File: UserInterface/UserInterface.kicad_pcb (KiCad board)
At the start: 2 copper layers, 102.2 x 65.5 mm, 30 parts, among them J1 Conn_01x18_Pin, SW0 RotaryEncoder_Switch_MP, SW1 SW_SPST, SW2 SW_SPST, SW3 SW_SPST, SW4 SW_SPST

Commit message: add main PCB
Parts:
- moved CSW4 22.0 mm to (153.5, 129.9)
- moved RSW4 22.0 mm to (153.5, 122.9)
- moved CSW3 20.8 mm to (147.3, 129.9)
- moved RSW3 20.8 mm to (147.3, 122.9)
- moved CSW2 19.5 mm to (141.0, 130.1)
- moved RSW2 19.5 mm to (141.0, 123.0)
- moved CSW0 19.5 mm to (117.0, 130.0)
- moved RSW0 19.5 mm to (117.0, 123.0)
- moved CSW1 18.5 mm to (135.0, 130.1)
- moved RSW1 18.5 mm to (135.0, 123.0)
- moved CSW0B1 18.5 mm to (123.0, 130.0)
- moved RSW0B1 18.5 mm to (123.0, 123.0)
- moved CSW0A1 17.5 mm to (129.0, 130.0)
- moved RSW0A1 17.5 mm to (129.0, 123.0)
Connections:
- J1 pad 10: /BUTTON_3 -> /RE_B
- J1 pad 11: /BUTTON_4 -> /LED_A
- J1 pad 12: /RE_SW -> /LED_B
- J1 pad 13: /RE_A -> /BUTTON_1
- J1 pad 14: /RE_B -> /BUTTON_2
- J1 pad 15: /LED_A -> /BUTTON_3
- J1 pad 16: /LED_B -> /BUTTON_4
- J1 pad 8: /BUTTON_1 -> /RE_SW
- J1 pad 9: /BUTTON_2 -> /RE_A
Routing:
- net GND: track 335.2 -> 235.7 mm, vias 3 -> 0
- net +5V: track 170.7 -> 82.8 mm, vias 1 -> 2
- net /RE_SW: track 37.2 -> 72.4 mm
- net /BUTTON_1: track 42.5 -> 69.1 mm
- net /BUTTON_2: track 28.3 -> 50.4 mm
- net /RE_A: track 65.9 -> 87.8 mm
- net /RE_B: track 53.2 -> 72.4 mm
- net /CS: track 54.8 -> 69.2 mm
- net /RES: track 53.9 -> 67.0 mm
- net /D: track 53.1 -> 64.6 mm
- net /LED_B: track 25.1 -> 35.2 mm, vias 1 -> 0
- net /SCK: track 52.2 -> 62.1 mm
- net /LED_A: track 23.1 -> 32.0 mm, vias 1 -> 0
- net /MOSI: track 51.6 -> 60.3 mm
- net /BUTTON_3: track 27.3 -> 35.9 mm
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
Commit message: ready to fix ui pcb
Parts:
- removed J1: Conn_01x18_Pin, Connector_PinHeader_2.54mm:PinHeader_1x18_P2.54mm_Vertical
- added J2: Conn_01x08_Pin, JST:JST-XH-08-PACKAGE-LONG-PAD, F.Cu at (71.1, 120.0)
- added J3: Conn_01x08_Pin, JST:JST-XH-08-PACKAGE-LONG-PAD, F.Cu at (71.1, 127.0)

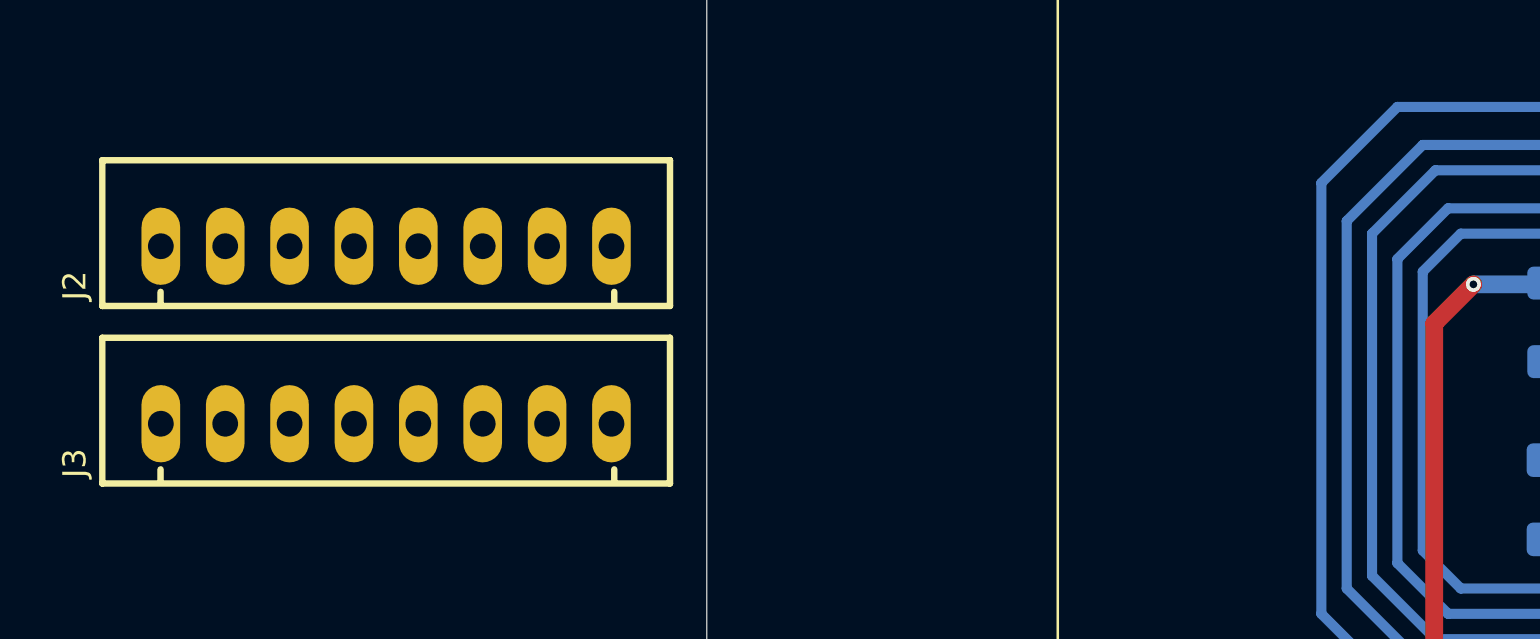
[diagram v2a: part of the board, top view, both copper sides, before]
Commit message: add step ui
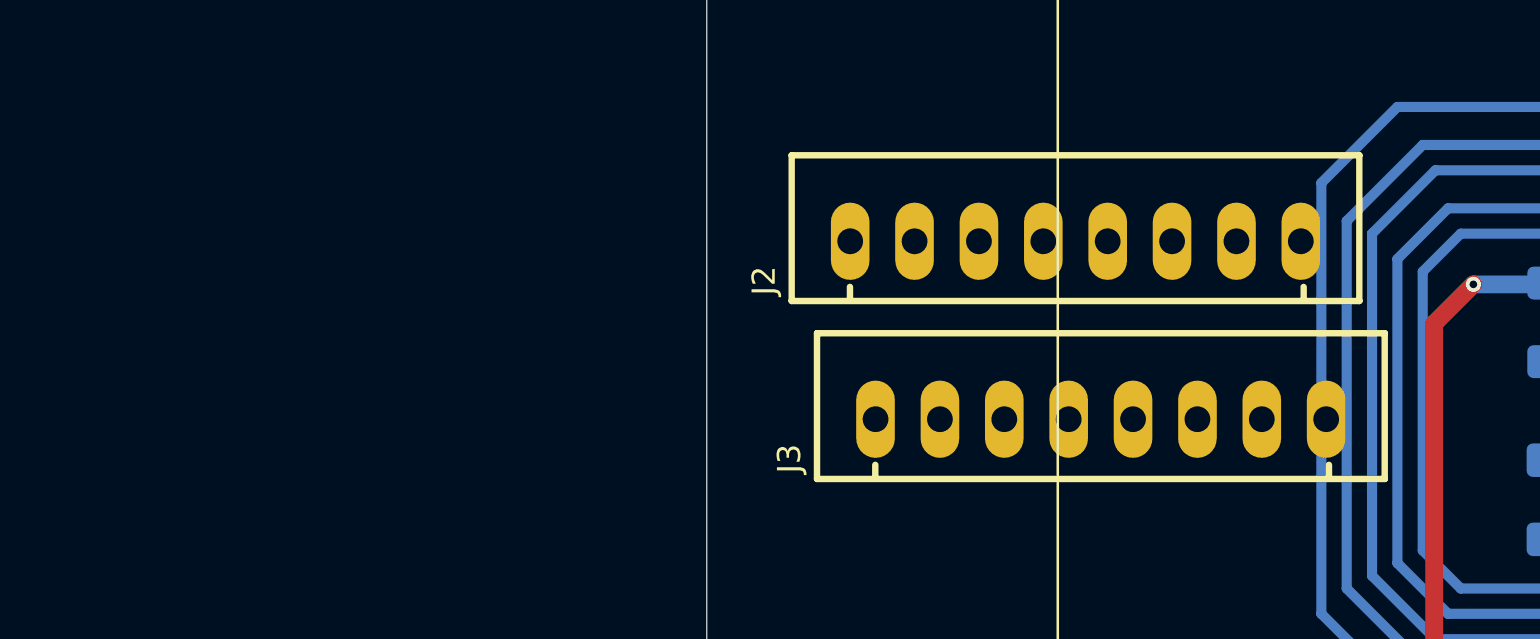
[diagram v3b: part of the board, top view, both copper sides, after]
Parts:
- moved J3 28.2 mm to (99.3, 126.8)
- moved J2 27.2 mm to (98.3, 119.8)
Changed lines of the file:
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@@
 	(footprint "JST:JST-XH-08-PACKAGE-LONG-PAD"
 		(layer "F.Cu")
-		(at 71.1 119.996)
+		(at 98.3 119.8)
 		(descr "JST XH Connector Long Pads (Package)\n\nWire to board connector.  Pitch: 2,54 mm, (0.100\")\n\nNumber of pins: 8  Created by Rembrandt Electronics\n\nwww.rembrandtelectronics.com")
 		(property "Reference" "J2"
@@
 	(footprint "JST:JST-XH-08-PACKAGE-LONG-PAD"
 		(layer "F.Cu")
-		(at 71.1 127)
+		(at 99.3 126.8215)
 		(descr "JST XH Connector Long Pads (Package)\n\nWire to board connector.  Pitch: 2,54 mm, (0.100\")\n\nNumber of pins: 8  Created by Rembrandt Electronics\n\nwww.rembrandtelectronics.com")
 		(property "Reference" "J3"
